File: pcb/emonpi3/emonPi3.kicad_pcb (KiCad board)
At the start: 4 copper layers, 85 x 88 mm, 186 parts, among them CN1 CONN_03SCREW, CN2 CONN_03SCREW, CN3 CONN_03SCREW, J1 SJ-3524-SMT-TR, J10 Conn_ARM_JTAG_SWD_10, J11 Conn_02x13_Odd_Even, J12 PINHD-1X9, J2 SJ-3524-SMT-TR, J3 SJ-3524-SMT-TR, J4 SJ-3524-SMT-TR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

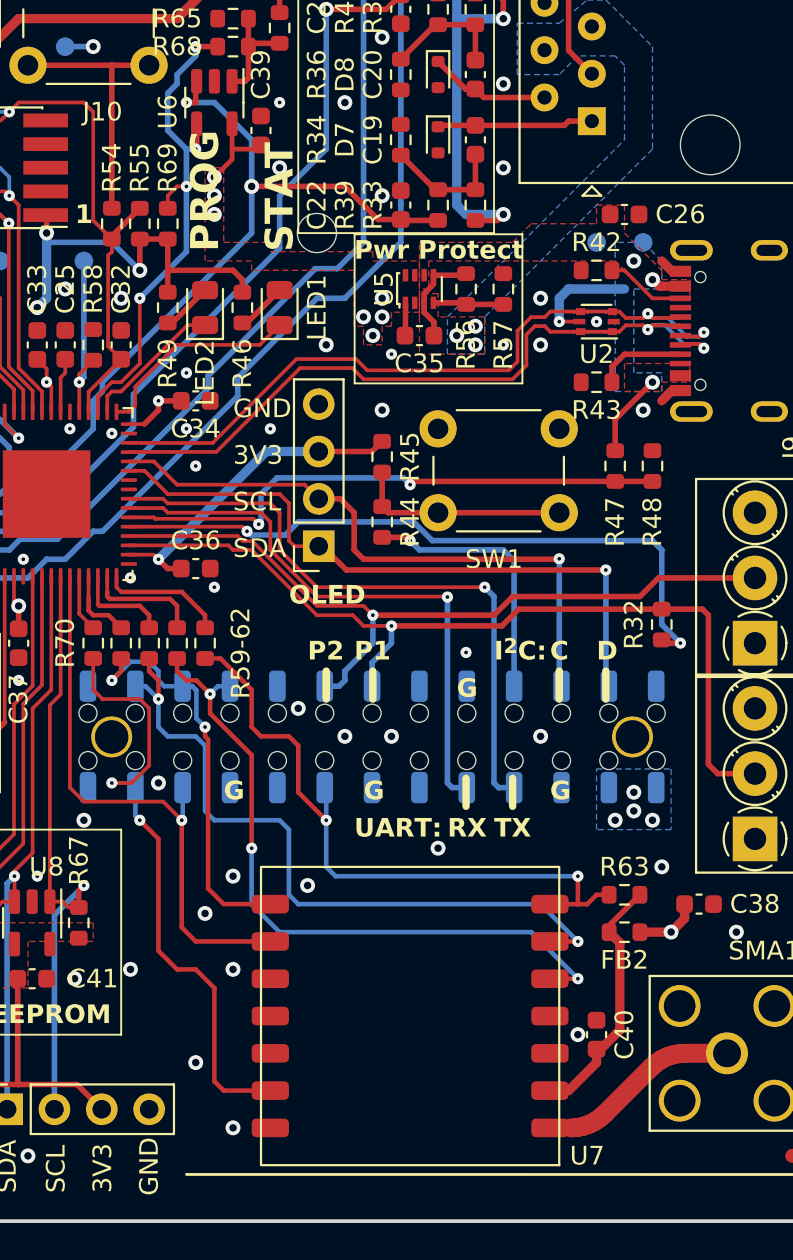
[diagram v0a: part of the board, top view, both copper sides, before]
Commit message: * Add mounting hole for external WiFi board
  - 2.5 mm diameter for (future) WiFi extender
  - Move RST and IRQ from RFM, label 26pin header
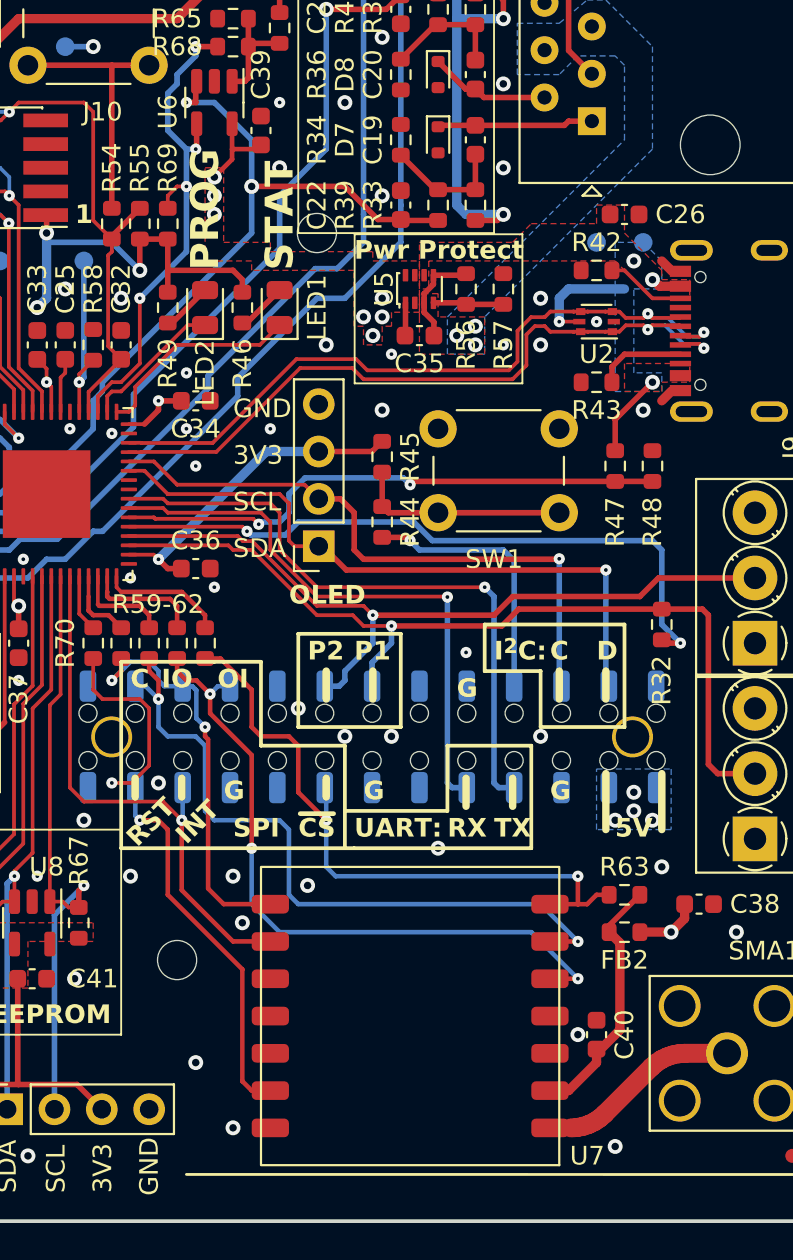
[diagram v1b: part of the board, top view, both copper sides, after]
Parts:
- added H8: MountingHole, MountingHole:MountingHole_2.1mm, F.Cu at (156.0, 136.0)
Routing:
- net /RFM_IRQ: track 30.6 -> 29.5 mm
- net /RFM_RESET: track 32.9 -> 32.0 mm
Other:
- board text added: "5V"
- board text added: "INT"
- board text added: "IO"
- board text added: "OI"
- board text added: "RST"
- board text added: "SPI"
- board text added: "~{CS}"

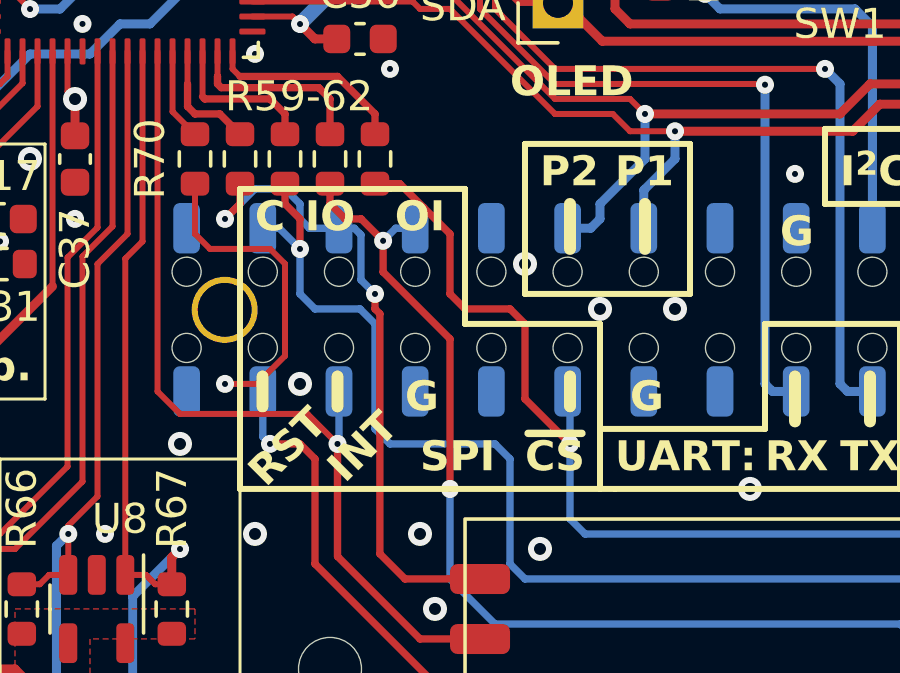
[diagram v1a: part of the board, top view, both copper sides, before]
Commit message: * Swap SPI MOSI and !SS pins, incorrect in v0.1
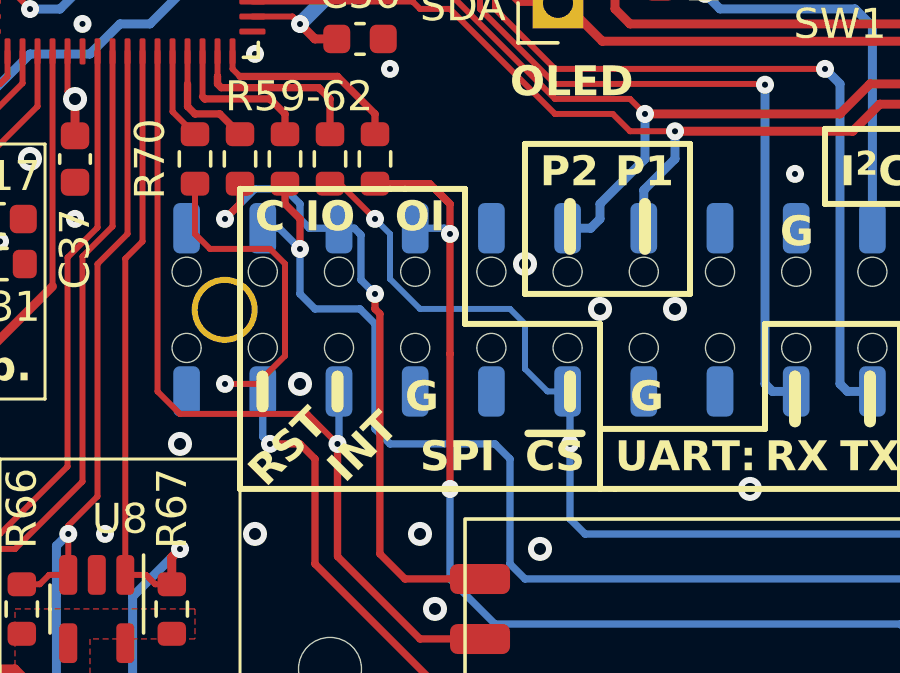
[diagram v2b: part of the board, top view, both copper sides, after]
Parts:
- moved R59 1.50 mm to (157.5, 119.0)
- moved R62 1.50 mm to (156.0, 119.0)
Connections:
- U3 pad 31: /RFM_MOSI_UC -> /RFM_SEL_UC
- U3 pad 32: /RFM_SEL_UC -> /RFM_MOSI_UC
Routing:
- net /RFM_MOSI: track 37.1 -> 37.9 mm
- net /RFM_SEL: track 35.5 -> 35.3 mm, vias 2 -> 3

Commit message: * Tidy up placement
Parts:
- moved R10 2.00 mm to (124.0, 76.5)
- moved C3 1.50 mm to (124.0, 79.5)
- moved C15 1.00 mm to (124.0, 142.0)
- moved R25 1.00 mm to (124.0, 138.5)
- moved R26 1.00 mm to (126.0, 142.0)
- moved R27 1.00 mm to (126.0, 138.5)
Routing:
- net Net-(C3-Pad2): track 6.50 -> 5.42 mm
- net Net-(D1-K): track 11.9 -> 12.5 mm

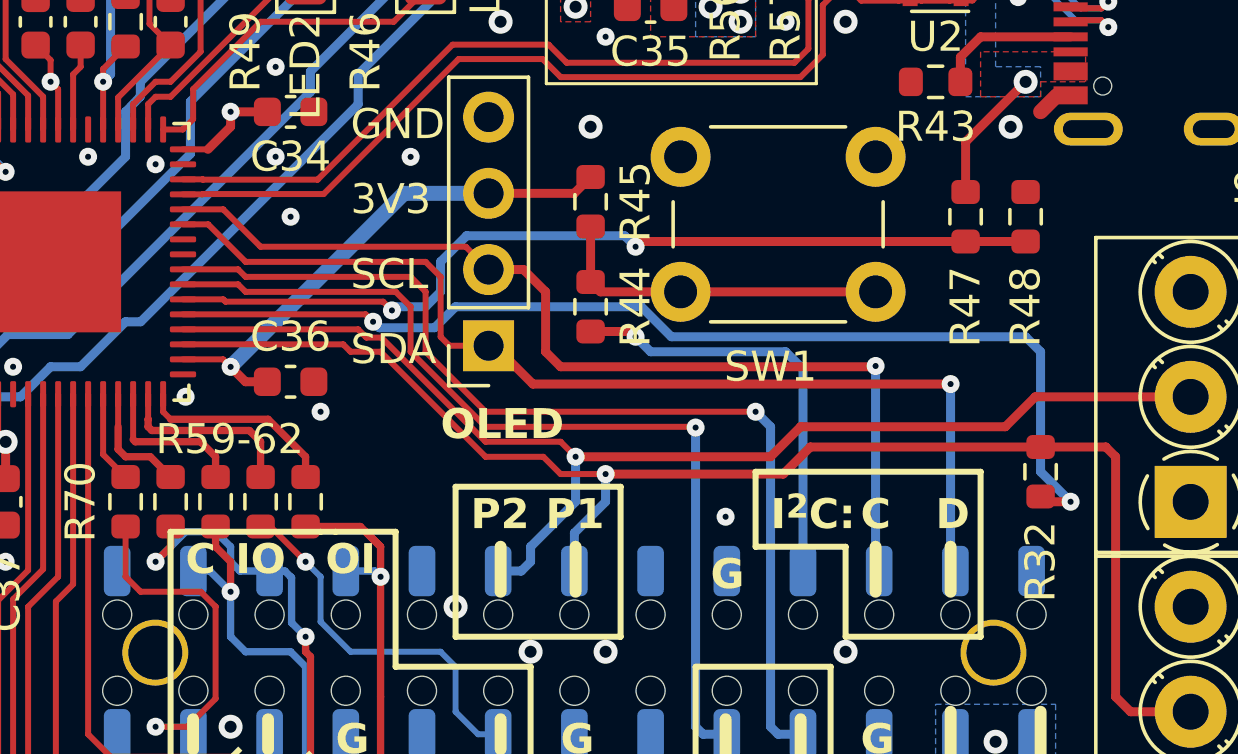
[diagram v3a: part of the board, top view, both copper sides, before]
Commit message: * Move external interface disable pin. Remove USB sense.
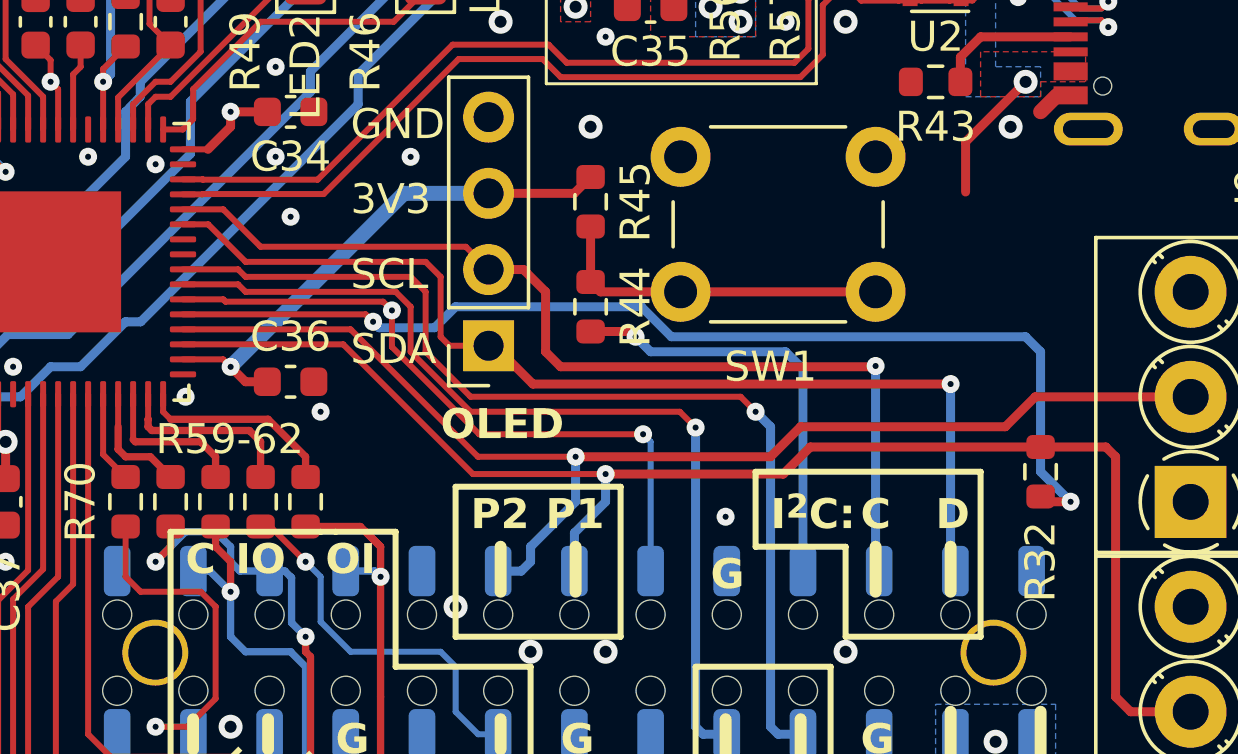
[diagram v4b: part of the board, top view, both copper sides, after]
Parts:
- removed R47, R48: 10K, Resistor_SMD:R_0603_1608Metric
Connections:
- J11 pad 11: unconnected-(J11-Pin_11-Pad11) -> /~{DISABLE_EXT_INTF}
- U3 pad 38: /VUSB_SENSE -> /~{DISABLE_EXT_INTF}
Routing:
- net /VUSB_SENSE: track 30.1 -> 0.00 mm, vias 2 -> 0
- net /~{DISABLE_EXT_INTF}: track 0.00 -> 22.6 mm, vias 0 -> 2
